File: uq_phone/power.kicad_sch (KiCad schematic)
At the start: 32 parts, among them J1 USB4105-GF-A, J2 S3B-PH-SM4-TB_LF__SN_, U1 MCP73871-2CCI_ML, U2 TPS62162DSGR, U3 BQ27441DRZR-G1A

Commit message: Update LCD, Add Programer, Shrink Footprints
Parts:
- R1, R10, R11, R2, R4, R5, R6, R7: footprint Resistor_SMD:R_0603_1608Metric -> Resistor_SMD:R_0402_1005Metric
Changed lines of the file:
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@@
 			)
 		)
-		(property "Footprint" "Resistor_SMD:R_0603_1608Metric"
+		(property "Footprint" "Resistor_SMD:R_0402_1005Metric"
 			(at 200.66 215.9 0)
 			(effects
@@
 			)
 		)
-		(property "Description" ""
+		(property "Description" "RES SMD 5.1K OHM 5% 1/10W 0402"
 			(at 200.66 215.9 0)
 			(effects
@@
 			)
 		)
-		(property "Footprint" "Resistor_SMD:R_0603_1608Metric"
+		(property "Footprint" "Resistor_SMD:R_0402_1005Metric"
 			(at 40.64 222.25 0)
 			(effects
@@
 			)
 		)
-		(property "Description" ""
+		(property "Description" "RES 100K OHM 1% 1/10W 0402"
 			(at 40.64 222.25 0)
 			(effects
@@
 			)
 		)
-		(property "Footprint" "Resistor_SMD:R_0603_1608Metric"
+		(property "Footprint" "Resistor_SMD:R_0402_1005Metric"
 			(at 66.04 60.96 0)
 			(effects
@@
 			)
 		)
-		(property "Description" ""
+		(property "Description" "RES SMD 5.1K OHM 5% 1/10W 0402"
 			(at 66.04 60.96 0)
 			(effects
@@
 			)
 		)
-		(property "Footprint" "Resistor_SMD:R_0603_1608Metric"
+		(property "Footprint" "Resistor_SMD:R_0402_1005Metric"
 			(at 231.14 53.34 0)
 			(effects
@@
 			)
 		)
-		(property "Description" ""
+		(property "Description" "RES 100K OHM 1% 1/10W 0402"
 			(at 231.14 53.34 0)
 			(effects
@@
 			)
 		)
-		(property "Footprint" "Resistor_SMD:R_0603_1608Metric"
+		(property "Footprint" "Resistor_SMD:R_0402_1005Metric"
 			(at 40.64 212.09 0)
 			(effects
@@
 			)
 		)
-		(property "Description" ""
+		(property "Description" "RES SMD 270K OHM 1% 1/10W 0402"
 			(at 40.64 212.09 0)
 			(effects
@@
 			)
 		)
-		(property "Footprint" "Resistor_SMD:R_0603_1608Metric"
+		(property "Footprint" "Resistor_SMD:R_0402_1005Metric"
 			(at 180.34 233.68 0)
 			(effects
@@
 			)
 		)
-		(property "Description" ""
+		(property "Description" "RES SMD 10K OHM 1% 1/10W 0402"
 			(at 180.34 233.68 0)
 			(effects
@@
 			)
 		)
-		(property "Footprint" "Resistor_SMD:R_0603_1608Metric"
+		(property "Footprint" "Resistor_SMD:R_0402_1005Metric"
 			(at 45.72 238.76 0)
 			(effects
@@
 			)
 		)
-		(property "Description" ""
+		(property "Description" "RES 100K OHM 1% 1/10W 0402"
 			(at 45.72 238.76 0)
 			(effects
@@
 			)
 		)
-		(property "Footprint" "Resistor_SMD:R_0603_1608Metric"
+		(property "Footprint" "Resistor_SMD:R_0402_1005Metric"
 			(at 57.15 60.96 0)
 			(effects
@@
 			)
 		)
-		(property "Description" ""
+		(property "Description" "RES SMD 5.1K OHM 5% 1/10W 0402"
 			(at 57.15 60.96 0)
 			(effects

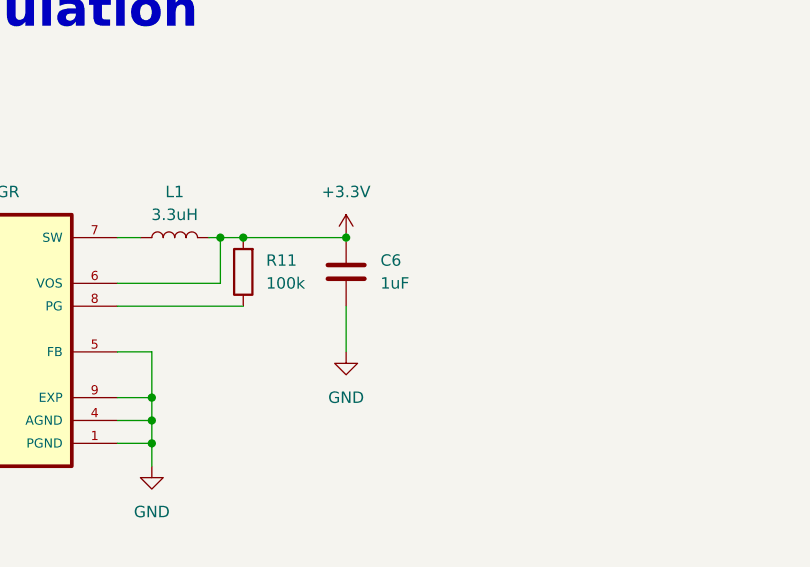
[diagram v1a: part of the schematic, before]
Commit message: Shrink More footprints, rearragment of PCB
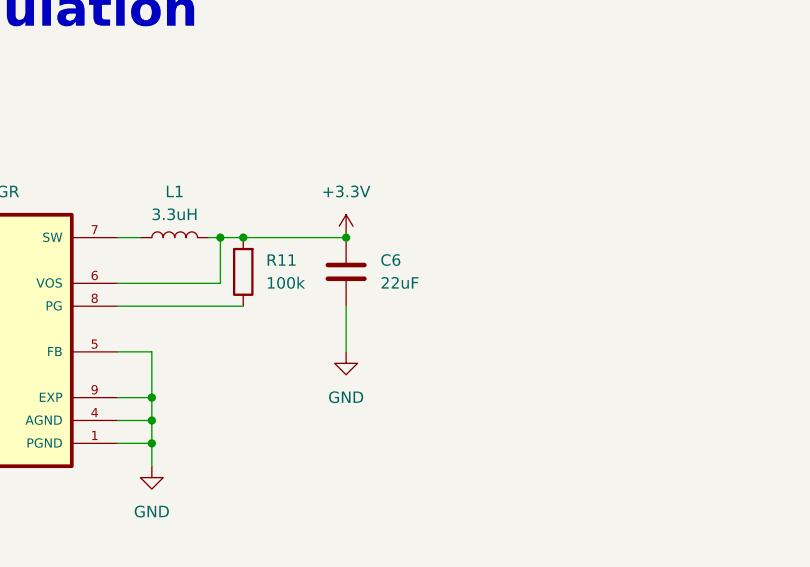
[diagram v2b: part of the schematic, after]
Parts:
- C2, C3, C5, C7: footprint Capacitor_SMD:C_0603_1608Metric -> Capacitor_SMD:C_0402_1005Metric
- C6: value 1uF -> 22uF
- R3: footprint Resistor_SMD:R_0603_1608Metric -> Resistor_SMD:R_0402_1005Metric
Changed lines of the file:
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@@
 	)
 	(junction
+		(at 242.57 45.72)
+		(diameter 0)
+		(color 0 0 0 0)
+	)
+	(junction
 		(at 83.82 39.37)
 		(diameter 0)
@@
 	)
 	(junction
-		(at 242.57 45.72)
-		(diameter 0)
-		(color 0 0 0 0)
-	)
-	(junction
 		(at 231.14 45.72)
 		(diameter 0)
@@
 			)
 		)
-		(property "Footprint" "Capacitor_SMD:C_0603_1608Metric"
+		(property "Footprint" "Capacitor_SMD:C_0402_1005Metric"
 			(at 240.03 222.25 0)
 			(effects
@@
 			)
 		)
-		(property "Description" ""
+		(property "Description" "CAP CER 470PF 10V X7R 0402"
 			(at 240.03 222.25 0)
 			(effects
@@
 			)
 		)
-		(property "Footprint" "Capacitor_SMD:C_0603_1608Metric"
+		(property "Footprint" "Capacitor_SMD:C_0402_1005Metric"
 			(at 67.31 252.73 0)
 			(effects
@@
 			)
 		)
-		(property "Description" ""
+		(property "Description" "4.7 µF ±10% 6.3V Ceramic Capacitor X5R 0402 (1005 Metric)"
 			(at 67.31 252.73 0)
 			(effects
@@
 			)
 		)
-		(property "Footprint" "Resistor_SMD:R_0603_1608Metric"
+		(property "Footprint" "Resistor_SMD:R_0402_1005Metric"
 			(at 40.64 231.14 0)
 			(effects
@@
 			)
 		)
-		(property "Description" ""
+		(property "Description" "RES SMD 1K OHM 1% 1/10W 0402"
 			(at 40.64 231.14 0)
 			(effects
@@
 			)
 		)
-		(property "Value" "1uF"
+		(property "Value" "22uF"
 			(at 246.38 50.7999 0)
 			(effects
@@
 			)
 		)
-		(property "Description" ""
+		(property "Description" "1 µF ±10% 25V Ceramic Capacitor X5R 0402 (1005 Metric)"
 			(at 242.57 49.53 0)
 			(effects
@@
 			)
 		)
-		(pin "1"
-		)
 		(pin "2"
 		)
+		(pin "1"
+		)
 		(instances
 			(project ""
@@
 			)
 		)
-		(property "Footprint" "Capacitor_SMD:C_0603_1608Metric"
+		(property "Footprint" "Capacitor_SMD:C_0402_1005Metric"
 			(at 242.57 240.03 0)
 			(effects
@@
 			)
 		)
-		(property "Description" ""
+		(property "Description" "1 µF ±10% 25V Ceramic Capacitor X5R 0402 (1005 Metric)"
 			(at 242.57 240.03 0)
 			(effects
@@
 			)
 		)
-		(property "Description" ""
+		(property "Description" "CAP CER 10UF 6.3V X5R 0603"
 			(at 58.42 209.55 0)
 			(effects
@@
 			)
 		)
-		(property "Footprint" "Capacitor_SMD:C_0603_1608Metric"
+		(property "Footprint" "Capacitor_SMD:C_0402_1005Metric"
 			(at 125.73 210.82 0)
 			(effects
@@
 			)
 		)
-		(property "Description" ""
+		(property "Description" "4.7 µF ±10% 6.3V Ceramic Capacitor X5R 0402 (1005 Metric)"
 			(at 125.73 210.82 0)
 			(effects
@@
 			)
 		)
-		(property "Description" ""
+		(property "Description" "CAP CER 10UF 6.3V X5R 0603"
 			(at 175.26 49.53 0)
 			(effects

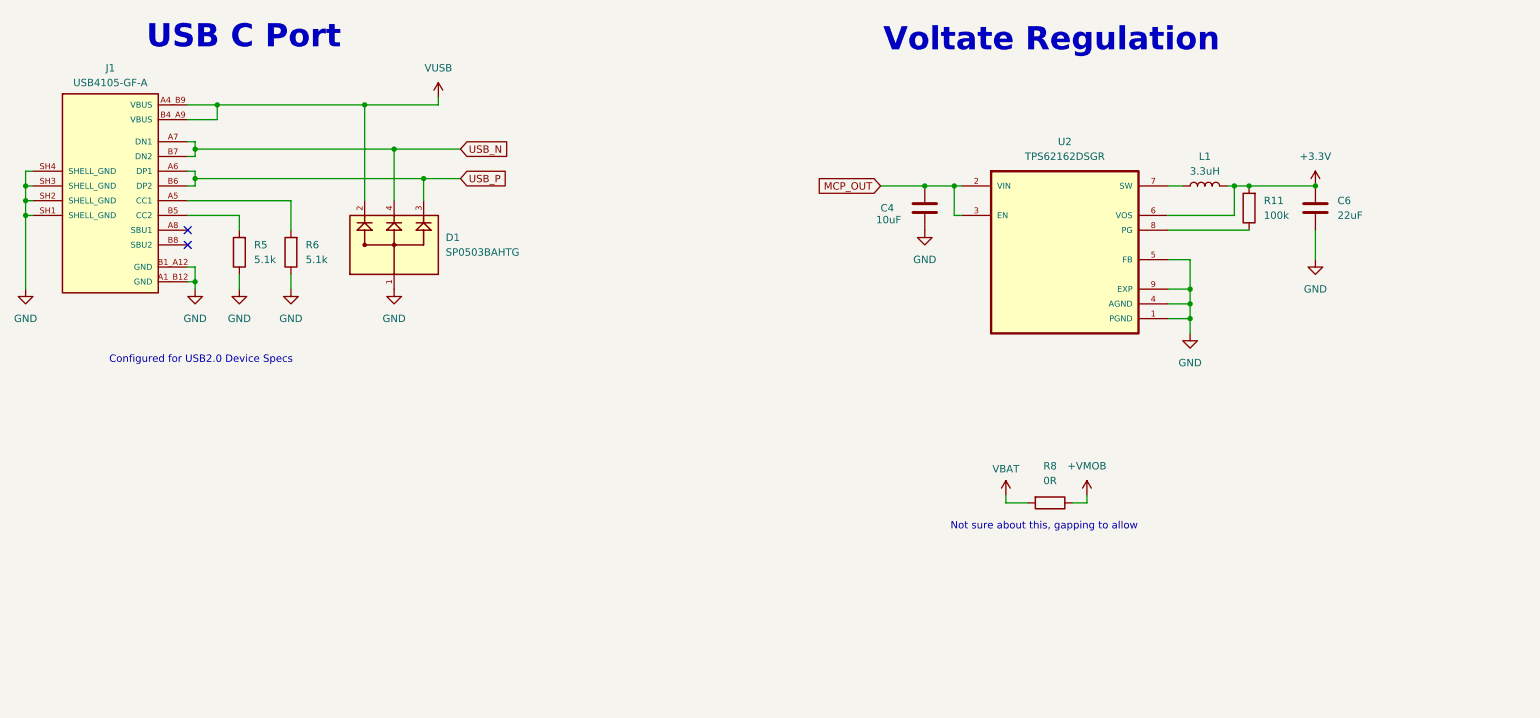
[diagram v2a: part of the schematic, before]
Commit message: Add LEDs, Inital Buttons
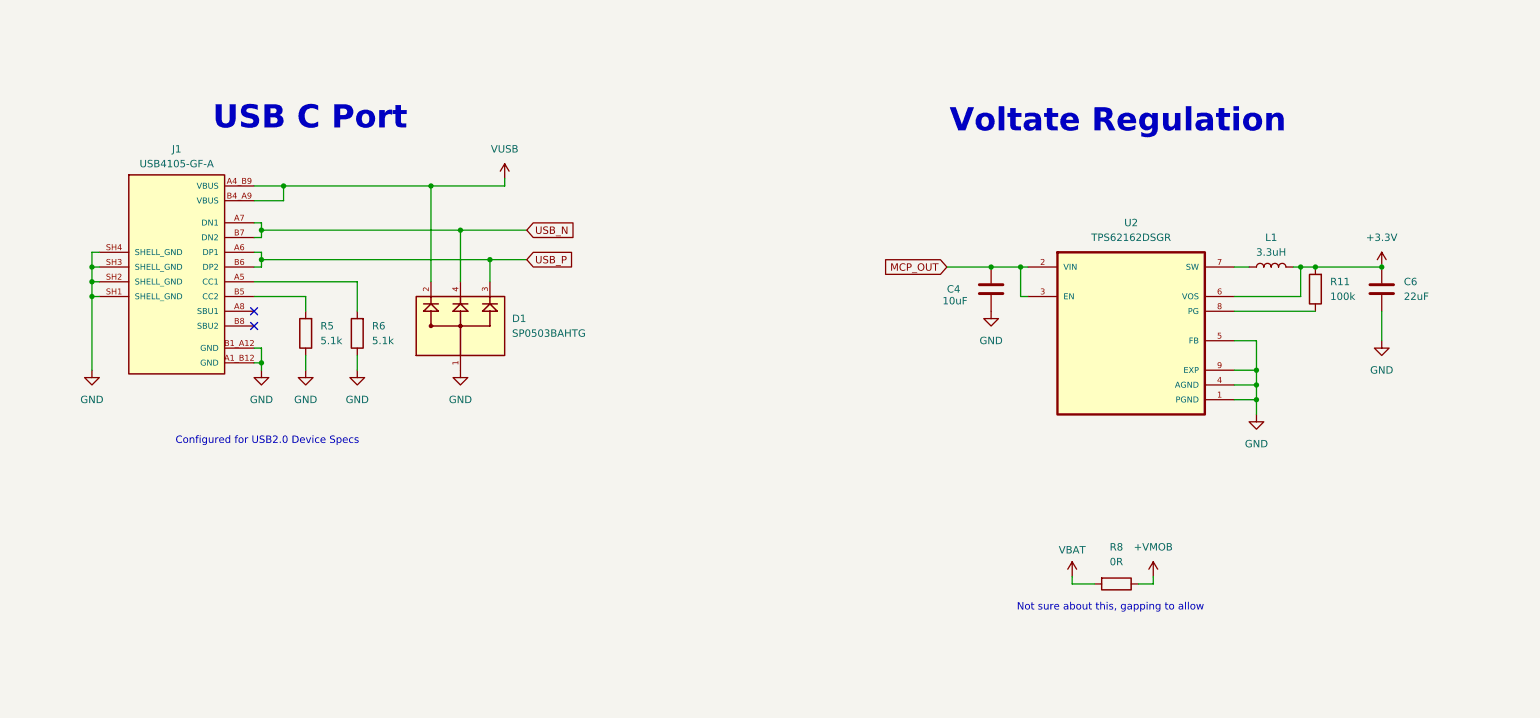
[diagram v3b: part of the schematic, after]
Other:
- moved on the sheet: C4, C6, D1, J1, L1, R11, R5, R6, R8, U2

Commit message: Routing Init
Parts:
- renumbered C7 to C6, C6 to C7, R8 to R10, R9 to R8, R10 to R9
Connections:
- net USB_N: now also D1.3; no longer D1.4
- net USB_P: now also D1.4; no longer D1.3
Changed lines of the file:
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@@
 	)
 	(junction
-		(at 95.25 53.34)
-		(diameter 0)
-		(color 0 0 0 0)
-	)
-	(junction
 		(at 40.64 213.36)
 		(diameter 0)
@@
 	)
 	(junction
-		(at 31.75 62.23)
+		(at 100.33 53.34)
 		(diameter 0)
 		(color 0 0 0 0)
 	)
 	(junction
-		(at 198.12 231.14)
+		(at 31.75 62.23)
 		(diameter 0)
 		(color 0 0 0 0)
 	)
 	(junction
-		(at 60.96 53.34)
+		(at 198.12 231.14)
 		(diameter 0)
 		(color 0 0 0 0)
 	)
 	(junction
-		(at 100.33 58.42)
+		(at 60.96 53.34)
 		(diameter 0)
 		(color 0 0 0 0)
@@
 	)
 	(junction
+		(at 95.25 58.42)
+		(diameter 0)
+		(color 0 0 0 0)
+	)
+	(junction
 		(at 240.03 59.69)
 		(diameter 0)
@@
 	(wire
 		(pts
+			(xy 100.33 53.34) (xy 106.68 53.34)
+		)
+		(stroke
+			(width 0)
+			(type default)
+		)
+	)
+	(wire
+		(pts
 			(xy 59.69 76.2) (xy 60.96 76.2)
 		)
@@
 	(wire
 		(pts
+			(xy 100.33 53.34) (xy 100.33 62.23)
+		)
+		(stroke
+			(width 0)
+			(type default)
+		)
+	)
+	(wire
+		(pts
 			(xy 59.69 45.72) (xy 64.77 45.72)
 		)
@@
 	(wire
 		(pts
-			(xy 100.33 58.42) (xy 100.33 62.23)
-		)
-		(stroke
-			(width 0)
-			(type default)
-		)
-	)
-	(wire
-		(pts
 			(xy 102.87 45.72) (xy 90.17 45.72)
 		)
@@
 	(wire
 		(pts
-			(xy 60.96 53.34) (xy 95.25 53.34)
+			(xy 60.96 53.34) (xy 100.33 53.34)
 		)
 		(stroke
@@
 	(wire
 		(pts
+			(xy 95.25 58.42) (xy 95.25 62.23)
+		)
+		(stroke
+			(width 0)
+			(type default)
+		)
+	)
+	(wire
+		(pts
 			(xy 228.6 72.39) (xy 232.41 72.39)
 		)
@@
 	(wire
 		(pts
-			(xy 95.25 53.34) (xy 106.68 53.34)
-		)
-		(stroke
-			(width 0)
-			(type default)
-		)
-	)
-	(wire
-		(pts
 			(xy 67.31 213.36) (xy 67.31 210.82)
 		)
@@
 	(wire
 		(pts
-			(xy 100.33 58.42) (xy 60.96 58.42)
+			(xy 60.96 58.42) (xy 95.25 58.42)
 		)
 		(stroke
@@
 	(wire
 		(pts
-			(xy 106.68 58.42) (xy 100.33 58.42)
-		)
-		(stroke
-			(width 0)
-			(type default)
-		)
-	)
-	(wire
-		(pts
 			(xy 198.12 238.76) (xy 203.2 238.76)
 		)
@@
 	(wire
 		(pts
-			(xy 95.25 62.23) (xy 95.25 53.34)
-		)
-		(stroke
-			(width 0)
-			(type default)
-		)
-	)
-	(wire
-		(pts
 			(xy 200.66 218.44) (xy 200.66 215.9)
 		)
@@
 	(wire
 		(pts
+			(xy 95.25 58.42) (xy 106.68 58.42)
+		)
+		(stroke
+			(width 0)
+			(type default)
+		)
+	)
+	(wire
+		(pts
 			(xy 187.96 248.92) (xy 182.88 248.92)
 		)
@@
 		(dnp no)
 		(fields_autoplaced yes)
-		(property "Reference" "#PWR027"
+		(property "Reference" "#PWR025"
 			(at 242.57 252.73 0)
 			(effects
@@
 			(project "uq_phone"
 				(path "/14f57415-6807-40a5-bb38-3cb818a2cdae/e697a7f0-03cd-4a38-a369-080a37468a6a"
-					(reference "#PWR027")
+					(reference "#PWR025")
 					(unit 1)
 				)
@@
 		(dnp no)
 		(fields_autoplaced yes)
-		(property "Reference" "#PWR012"
+		(property "Reference" "#PWR010"
 			(at 67.31 262.89 0)
 			(effects
@@
 			(project "uq_phone"
 				(path "/14f57415-6807-40a5-bb38-3cb818a2cdae/e697a7f0-03cd-4a38-a369-080a37468a6a"
-					(reference "#PWR012")
+					(reference "#PWR010")
 					(unit 1)
 				)
@@
 		(on_board yes)
 		(dnp no)
-		(property "Reference" "R10"
+		(property "Reference" "R9"
 			(at 201.93 210.058 0)
 			(effects
@@
 			(project "uq_phone"
 				(path "/14f57415-6807-40a5-bb38-3cb818a2cdae/e697a7f0-03cd-4a38-a369-080a37468a6a"
-					(reference "R10")
+					(reference "R9")
 					(unit 1)
 				)
@@
 		(dnp no)
 		(fields_autoplaced yes)
-		(property "Reference" "#PWR025"
+		(property "Reference" "#PWR027"
 			(at 254 63.5 0)
 			(effects
@@
 			(project "uq_phone"
 				(path "/14f57415-6807-40a5-bb38-3cb818a2cdae/e697a7f0-03cd-4a38-a369-080a37468a6a"
-					(reference "#PWR025")
+					(reference "#PWR027")
 					(unit 1)
 				)
@@
 		(on_board yes)
 		(dnp no)
-		(property "Reference" "#PWR011"
+		(property "Reference" "#PWR09"
 			(at 67.31 243.84 0)
 			(effects
@@
 			(project "uq_phone"
 				(path "/14f57415-6807-40a5-bb38-3cb818a2cdae/e697a7f0-03cd-4a38-a369-080a37468a6a"
-					(reference "#PWR011")
+					(reference "#PWR09")
 					(unit 1)
 				)
@@
 		(on_board yes)
 		(dnp no)
-		(property "Reference" "#PWR018"
+		(property "Reference" "#PWR017"
 			(at 180.34 240.03 0)
 			(effects
@@
 			(project "uq_phone"
 				(path "/14f57415-6807-40a5-bb38-3cb818a2cdae/e697a7f0-03cd-4a38-a369-080a37468a6a"
-					(reference "#PWR018")
+					(reference "#PWR017")
 					(unit 1)
 				)
@@
 		(dnp no)
 		(fields_autoplaced yes)
-		(property "Reference" "C6"
+		(property "Reference" "C7"
 			(at 257.81 62.2299 0)
 			(effects
@@
 			(project ""
 				(path "/14f57415-6807-40a5-bb38-3cb818a2cdae/e697a7f0-03cd-4a38-a369-080a37468a6a"
-					(reference "C6")
+					(reference "C7")
 					(unit 1)
 				)
@@
 		(dnp no)
 		(fields_autoplaced yes)
-		(property "Reference" "#PWR017"
+		(property "Reference" "#PWR018"
 			(at 186.69 73.66 0)
 			(effects
@@
 			(project "uq_phone"
 				(path "/14f57415-6807-40a5-bb38-3cb818a2cdae/e697a7f0-03cd-4a38-a369-080a37468a6a"
-					(reference "#PWR017")
+					(reference "#PWR018")
 					(unit 1)
 				)
@@
 		(on_board yes)
 		(dnp no)
-		(property "Reference" "#PWR08"
+		(property "Reference" "#PWR06"
 			(at 58.42 220.98 0)
 			(effects
@@
 			(project "uq_phone"
 				(path "/14f57415-6807-40a5-bb38-3cb818a2cdae/e697a7f0-03cd-4a38-a369-080a37468a6a"
-					(reference "#PWR08")
+					(reference "#PWR06")
 					(unit 1)
 				)
@@
 		(on_board yes)
 		(dnp no)
-		(property "Reference" "#PWR021"
+		(property "Reference" "#PWR020"
 			(at 198.12 233.68 0)
 			(effects
@@
 			(project "uq_phone"
 				(path "/14f57415-6807-40a5-bb38-3cb818a2cdae/e697a7f0-03cd-4a38-a369-080a37468a6a"
-					(reference "#PWR021")
+					(reference "#PWR020")
 					(unit 1)
 				)
@@
 		(dnp no)
 		(fields_autoplaced yes)
-		(property "Reference" "#PWR09"
+		(property "Reference" "#PWR012"
 			(at 77.47 83.82 0)
 			(effects
@@
 			(project "uq_phone"
 				(path "/14f57415-6807-40a5-bb38-3cb818a2cdae/e697a7f0-03cd-4a38-a369-080a37468a6a"
-					(reference "#PWR09")
+					(reference "#PWR012")
 					(unit 1)
 				)
@@
 		(dnp no)
 		(fields_autoplaced yes)
-		(property "Reference" "R8"
+		(property "Reference" "R10"
 			(at 208.28 107.95 90)
 			(effects
@@
 			(project ""
 				(path "/14f57415-6807-40a5-bb38-3cb818a2cdae/e697a7f0-03cd-4a38-a369-080a37468a6a"
-					(reference "R8")
+					(reference "R10")
 					(unit 1)
 				)
@@
 		(on_board yes)
 		(dnp no)
-		(property "Reference" "#PWR010"
+		(property "Reference" "#PWR08"
 			(at 67.31 231.14 0)
 			(effects
@@
 			(project "uq_phone"
 				(path "/14f57415-6807-40a5-bb38-3cb818a2cdae/e697a7f0-03cd-4a38-a369-080a37468a6a"
-					(reference "#PWR010")
+					(reference "#PWR08")
 					(unit 1)
 				)
@@
 		(dnp no)
 		(fields_autoplaced yes)
-		(property "Reference" "#PWR028"
+		(property "Reference" "#PWR026"
 			(at 248.92 236.22 0)
 			(effects
@@
 			(project "uq_phone"
 				(path "/14f57415-6807-40a5-bb38-3cb818a2cdae/e697a7f0-03cd-4a38-a369-080a37468a6a"
-					(reference "#PWR028")
+					(reference "#PWR026")
 					(unit 1)
 				)
@@
 		(dnp no)
 		(fields_autoplaced yes)
-		(property "Reference" "#PWR06"
+		(property "Reference" "#PWR011"
 			(at 68.58 83.82 0)
 			(effects
@@
 			(project "uq_phone"
 				(path "/14f57415-6807-40a5-bb38-3cb818a2cdae/e697a7f0-03cd-4a38-a369-080a37468a6a"
-					(reference "#PWR06")
+					(reference "#PWR011")
 					(unit 1)
 				)
@@
 		(on_board yes)
 		(dnp no)
-		(property "Reference" "R9"
+		(property "Reference" "R8"
 			(at 192.532 233.68 0)
 			(effects
@@
 			(project ""
 				(path "/14f57415-6807-40a5-bb38-3cb818a2cdae/e697a7f0-03cd-4a38-a369-080a37468a6a"
-					(reference "R9")
+					(reference "R8")
 					(unit 1)
 				)
@@
 		(dnp no)
 		(fields_autoplaced yes)
-		(property "Reference" "#PWR05"
+		(property "Reference" "#PWR07"
 			(at 60.96 83.82 0)
 			(effects
@@
 			(project "uq_phone"
 				(path "/14f57415-6807-40a5-bb38-3cb818a2cdae/e697a7f0-03cd-4a38-a369-080a37468a6a"
-					(reference "#PWR05")
+					(reference "#PWR07")
 					(unit 1)
 				)
@@
 		(dnp no)
 		(fields_autoplaced yes)
-		(property "Reference" "#PWR07"
+		(property "Reference" "#PWR05"
 			(at 58.42 205.74 0)
 			(effects
@@
 			(project "uq_phone"
 				(path "/14f57415-6807-40a5-bb38-3cb818a2cdae/e697a7f0-03cd-4a38-a369-080a37468a6a"
-					(reference "#PWR07")
+					(reference "#PWR05")
 					(unit 1)
 				)
@@
 		(on_board yes)
 		(dnp no)
-		(property "Reference" "C7"
+		(property "Reference" "C6"
 			(at 245.872 238.76 0)
 			(effects
@@
 			(project ""
 				(path "/14f57415-6807-40a5-bb38-3cb818a2cdae/e697a7f0-03cd-4a38-a369-080a37468a6a"
-					(reference "C7")
+					(reference "C6")
 					(unit 1)
 				)
@@
 		(on_board yes)
 		(dnp no)
-		(property "Reference" "#PWR020"
+		(property "Reference" "#PWR021"
 			(at 200.66 116.84 0)
 			(effects
@@
 			(project "uq_phone"
 				(path "/14f57415-6807-40a5-bb38-3cb818a2cdae/e697a7f0-03cd-4a38-a369-080a37468a6a"
-					(reference "#PWR020")
+					(reference "#PWR021")
 					(unit 1)
 				)
@@
 		(dnp no)
 		(fields_autoplaced yes)
-		(property "Reference" "#PWR026"
+		(property "Reference" "#PWR028"
 			(at 254 78.74 0)
 			(effects
@@
 			(project "uq_phone"
 				(path "/14f57415-6807-40a5-bb38-3cb818a2cdae/e697a7f0-03cd-4a38-a369-080a37468a6a"
-					(reference "#PWR026")
+					(reference "#PWR028")
 					(unit 1)
 				)

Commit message: Update pcb and remove Stm32 profile
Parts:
- U1: Description_1 Microchip MCP73871-2CCI/ML, Battery Charge Controller, 1000mA, 20-Pin QFN | Microchip Technology Inc. MCP73871-2CCI/ML -> Microchip MCP73871-2CCI/ML, Battery Charge Controller, 1000mA, 20-Pin QFN | Microchip Technology Inc. MCP73871-2CCI/ML
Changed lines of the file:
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@@
 			)
 		)
-		(property "Description_1" "\n                        \n                            Microchip MCP73871-2CCI/ML, Battery Charge Controller, 1000mA, 20-Pin QFN | Microchip Technology Inc. MCP73871-2CCI/ML\n                        \n"
+		(property "Description_1" "Microchip MCP73871-2CCI/ML, Battery Charge Controller, 1000mA, 20-Pin QFN | Microchip Technology Inc. MCP73871-2CCI/ML"
 			(at 87.63 226.06 0)
 			(effects

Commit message: Swap RX TX
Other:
- note added: "Charge Rate. =1000/RProg1 = 1A"
- note added: "Charge terminiation when I = 1000/Rprog3 = 10mA"
- note added: "Configured for USB2.0 Device Specs for max current sink"
- note added: "Reduce Battery charge if Vin falls below 5 * (270/(270 + 100)) V = 3.6V"
- note removed: "Battery Status Ensure all have pull-ups either external or interanl to MCU Can also use LED for some status LED maybe"
- note removed: "Charge Rate. Eq = 1000/RProg1"
- note removed: "Configured for USB2.0 Device Specs"
- moved on the sheet: D1, J1, R10, R5, R6, TP6
